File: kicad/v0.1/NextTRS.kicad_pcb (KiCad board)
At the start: 2 copper layers, 145.7 x 107.8 mm, 98 parts, among them J1 TRS-80 M3 Pin Header, J10 AudioJack3, J11 Mini-DIN-6, J12 USB_B_Micro, J2 TRS-80 M1 Pin Connector, J3 TRS-80 M3 Edge Connector, J4 TRS-80 M1 Edge Connector, J5 Conn_01x06_Male, J6 Conn_01x06_Male, J7 HDMI_A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

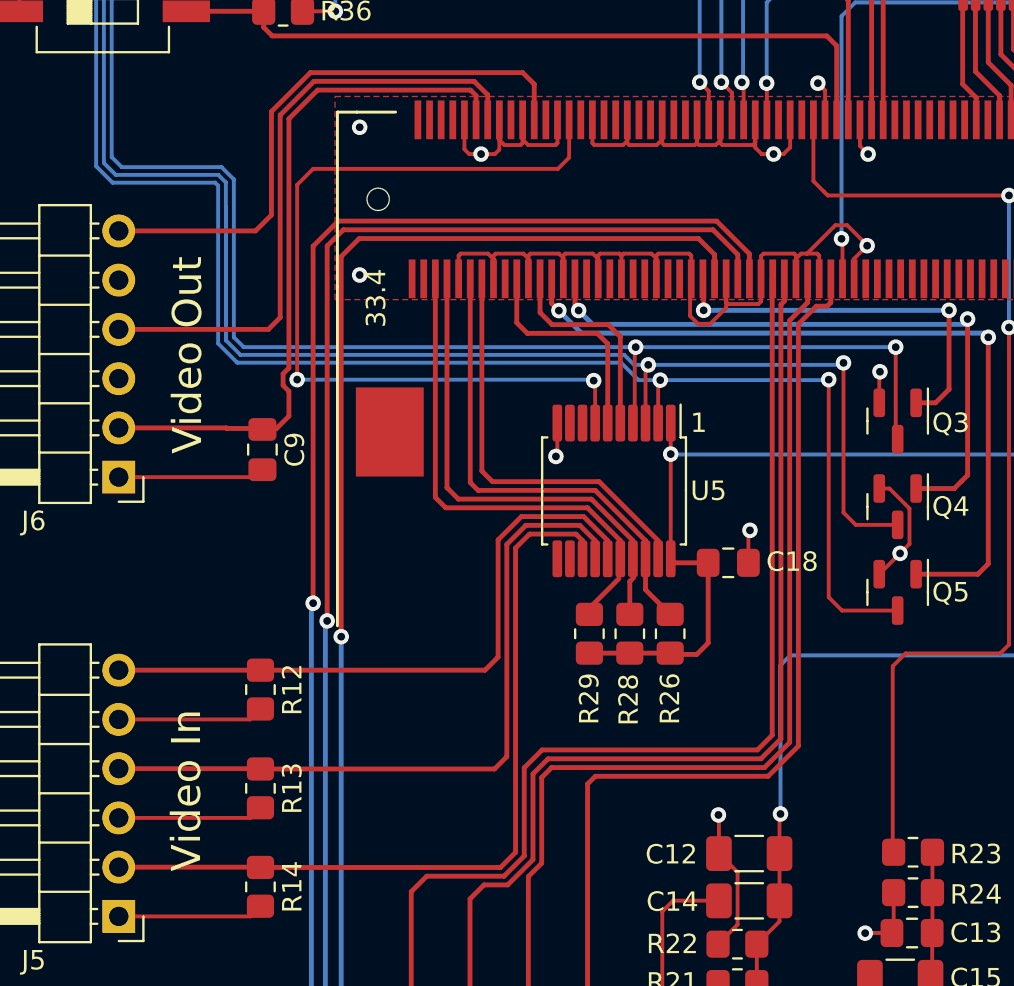
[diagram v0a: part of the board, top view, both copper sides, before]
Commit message: New routing for U5
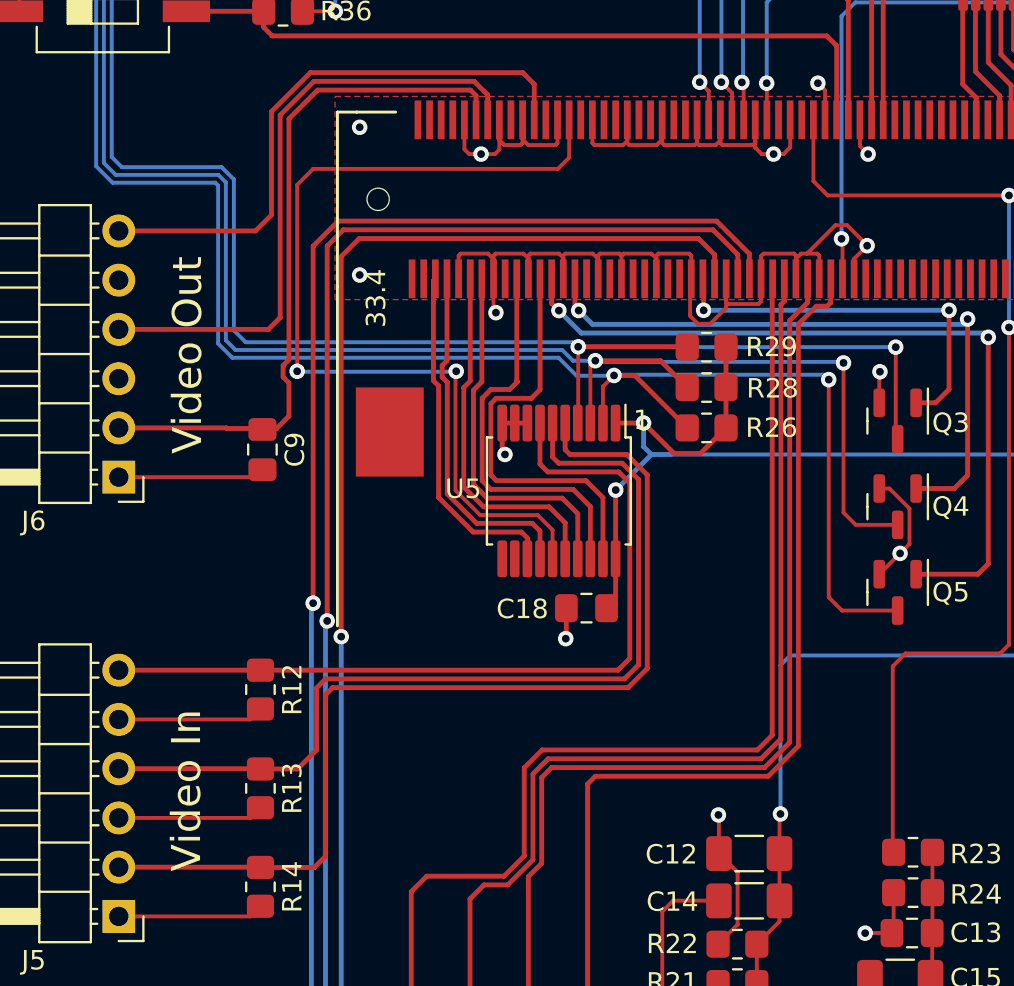
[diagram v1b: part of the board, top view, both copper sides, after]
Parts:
- moved R29 16.0 mm to (62.0, 101.2), turned to 180 degrees
- moved R28 13.3 mm to (62.0, 103.3), turned to 180 degrees
- moved R26 10.8 mm to (62.0, 105.4), turned to 180 degrees
- moved C18 7.68 mm to (55.8, 114.7), turned to 180 degrees
- moved U5 2.84 mm to (54.4, 108.6)
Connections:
- Conn1 pad 182: HSYNCX -> CTRL1_EN
- Conn1 pad 186: VSYNCX -> EXTIOSEL_IN_N
- Conn1 pad 192: CTRL1_EN -> WAIT_IN_N
- Conn1 pad 194: EXTIOSEL_IN_N -> INT_IN_N
- Conn1 pad 198: WAIT_IN_N -> VSYNCX
- Conn1 pad 200: INT_IN_N -> HSYNCX
- U5 pad 13: VIDEOX -> HSYNCX
- U5 pad 15: HSYNCX -> VIDEOX
- U5 pad 5: HSYNC -> VIDEO
- U5 pad 7: VIDEO -> HSYNC
- U5 pad 8: unconnected-(U5-Pad8) -> GND
- U5 pad 9: unconnected-(U5-Pad9) -> GND
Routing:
- net VIDEOX: track 0.00 -> 47.9 mm, vias 0 -> 2
- net VIDEO: track 85.5 -> 52.5 mm, vias 2 -> 0
- net VSYNC: track 37.5 -> 47.1 mm
- net HSYNC: track 33.5 -> 42.8 mm
- net HSYNCX: track 10.9 -> 17.9 mm
- net VSYNCX: track 11.5 -> 18.3 mm
- net INT_IN_N: track 25.2 -> 18.7 mm
- net WAIT_N: track 241.6 -> 247.1 mm
- net INT_N: track 222.0 -> 227.4 mm
- net EXTIOSEL_N: track 169.4 -> 174.7 mm
- net WAIT_IN_N: track 24.4 -> 19.1 mm
- net EXTIOSEL_IN_N: track 25.1 -> 20.6 mm
- net +3V3: track 335.4 -> 338.5 mm, vias 11 -> 12
- net GND: track 555.5 -> 558.4 mm, vias 43 -> 44

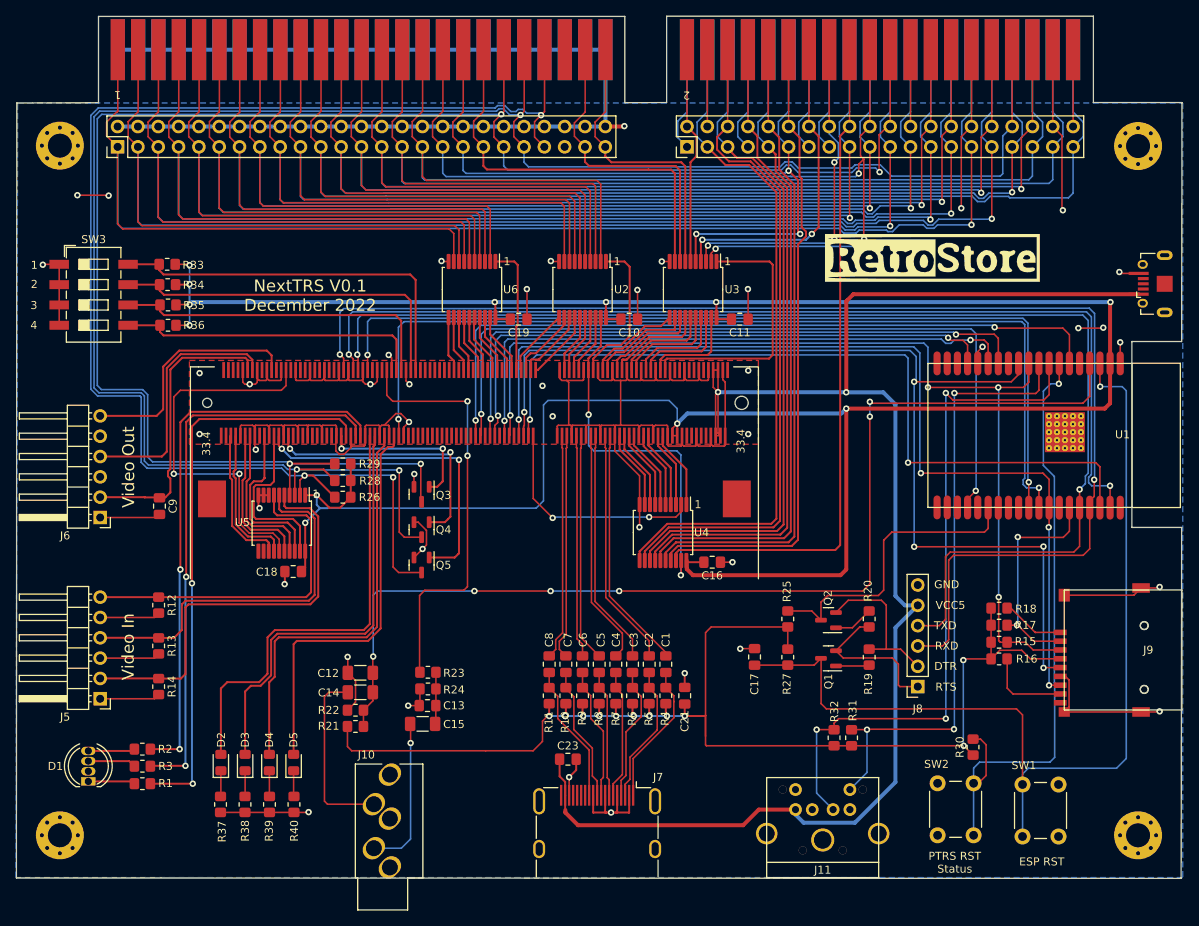
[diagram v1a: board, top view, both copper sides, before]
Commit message: Stiffened grounds around TRS-80 connectors.
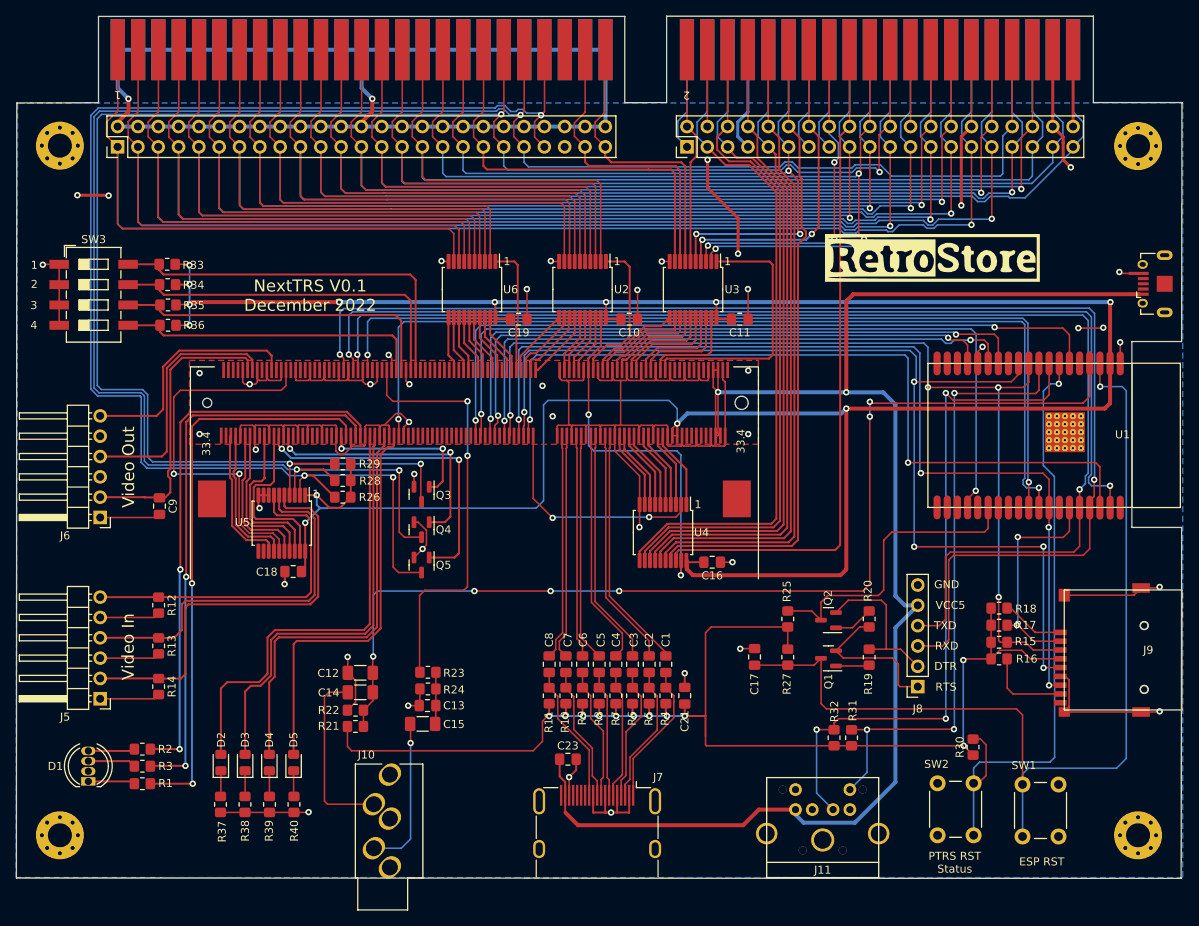
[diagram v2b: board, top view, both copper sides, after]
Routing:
- net GND: track 558.4 -> 550.3 mm, vias 44 -> 47
- net A2: track 178.3 -> 174.8 mm
- net IN_N: track 116.2 -> 114.3 mm
- net SCK: track 131.8 -> 130.4 mm
- net A6: track 154.6 -> 153.3 mm
- net ESP_S3: track 97.2 -> 96.2 mm
- net TXD0: track 164.3 -> 163.4 mm
- net BUTTON: track 78.1 -> 77.5 mm
- net INT_N: track 227.4 -> 226.8 mm
- net +3.3V: track 156.5 -> 156.3 mm, vias 12 -> 11
- net +3V3: track 338.5 -> 338.4 mm, vias 12 -> 13
